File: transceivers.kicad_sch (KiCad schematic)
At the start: 18 parts, among them U401 TLE9351VSJ, U402 TLE7258SJ

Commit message: completed schematic
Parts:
- removed D33: BAT60A, Diode_SMD:D_SOD-323, symbol Diode:BAT60A
- added D513: PMEG4010CEH, Diode_SMD:D_SOD-123F, symbol Diode:PMEG4010CEH
- D401: value D_TVS_Dual_AAC -> PESD2CANFD24V-T
- FL401: value Filter_EMI_LL_1423 -> WE 744222
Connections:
- net Vdrive: now also D513.2 (A)
- net at R406.1: now also D513.1 (K)
- net +3V3 renamed +3.3V
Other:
- note removed: "ToDo: Drossel dimensionieren (Würth 744222?) TVS: PESD1CAN einfügen"
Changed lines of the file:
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@@
 (kicad_sch (version 20230121) (generator eeschema)
   (paper "A4")
+  (bus_alias "CAN" (members "CAN_TX" "CAN_RX" "CAN_STBY"))
   (bus_alias "Comm" (members "CAN_H" "CAN_L" "LIN"))
-  (bus_alias "CAN" (members "CAN_TX" "CAN_RX" "CAN_STBY"))
+  (bus_alias "Power_OUT" (members "Half0_OUT" "Half1_OUT" "1A_Out0" "1A_Out2" "1A_Out3" "1A_Out1" ""))
   (bus_alias "LIN" (members "LIN_TX" "LIN_RX" "LIN_EN"))
-  (bus_alias "Power_OUT" (members "Half0_OUT" "Half1_OUT" "1A_Out0" "1A_Out2" "1A_Out3" "1A_Out1" ""))
   (junction (at 166.37 99.06) (diameter 0) (color 0 0 0 0)
   )
@@
   (wire (pts (xy 58.42 58.42) (xy 71.12 58.42))
     (stroke (width 0) (type default))
-  )
-  (text "ToDo:\nDrossel dimensionieren (Würth 744222?)\nTVS: PESD1CAN einfügen"
-    (at 189.23 59.69 0)
-    (effects (font (size 1.27 1.27)) (justify left bottom))
   )
   (label "LIN_EN" (at 106.68 99.06 0) (fields_autoplaced)
@@
     )
   )
-  (symbol (lib_id "Device:R") (at 191.77 44.45 0) (unit 1)
-    (in_bom yes) (on_board yes) (dnp no) (fields_autoplaced)
-    (property "Reference" "R403" (at 194.31 43.1799 0)
-      (effects (font (size 1.27 1.27)) (justify left))
-    )
-    (property "Value" "60" (at 194.31 45.7199 0)
-      (effects (font (size 1.27 1.27)) (justify left))
-    )
-    (property "Footprint" "Resistor_SMD:R_0603_1608Metric" (at 189.992 44.45 90)
+  (symbol (lib_id "Device:R") (at 191.77 44.45 0) (mirror y) (unit 1)
+    (in_bom yes) (on_board yes) (dnp no)
+    (property "Reference" "R403" (at 189.23 43.1799 0)
+      (effects (font (size 1.27 1.27)) (justify left))
+    )
+    (property "Value" "60" (at 189.23 45.7199 0)
+      (effects (font (size 1.27 1.27)) (justify left))
+    )
+    (property "Footprint" "Resistor_SMD:R_0603_1608Metric" (at 193.548 44.45 90)
       (effects (font (size 1.27 1.27)) hide)
     )
@@
   )
   (symbol (lib_id "Device:Filter_EMI_LL_1423") (at 172.72 38.1 0) (unit 1)
-    (in_bom yes) (on_board yes) (dnp no) (fields_autoplaced)
-    (property "Reference" "FL401" (at 172.339 30.48 0)
-      (effects (font (size 1.27 1.27)))
-    )
-    (property "Value" "Filter_EMI_LL_1423" (at 172.339 33.02 0)
+    (in_bom yes) (on_board yes) (dnp no)
+    (property "Reference" "FL401" (at 172.72 43.18 0)
+      (effects (font (size 1.27 1.27)))
+    )
+    (property "Value" "WE 744222" (at 172.72 45.72 0)
       (effects (font (size 1.27 1.27)))
     )
@@
     )
   )
-  (symbol (lib_id "Device:R") (at 172.72 50.8 90) (unit 1)
-    (in_bom yes) (on_board yes) (dnp yes) (fields_autoplaced)
-    (property "Reference" "R404" (at 172.72 44.45 90)
-      (effects (font (size 1.27 1.27)))
-    )
-    (property "Value" "0" (at 172.72 46.99 90)
-      (effects (font (size 1.27 1.27)))
-    )
-    (property "Footprint" "Resistor_SMD:R_0603_1608Metric" (at 172.72 52.578 90)
+  (symbol (lib_id "Device:R") (at 172.72 50.8 90) (mirror x) (unit 1)
+    (in_bom yes) (on_board yes) (dnp yes)
+    (property "Reference" "R404" (at 172.72 57.15 90)
+      (effects (font (size 1.27 1.27)))
+    )
+    (property "Value" "0" (at 172.72 54.61 90)
+      (effects (font (size 1.27 1.27)))
+    )
+    (property "Footprint" "Resistor_SMD:R_0603_1608Metric" (at 172.72 49.022 90)
       (effects (font (size 1.27 1.27)) hide)
     )
@@
   )
   (symbol (lib_id "Device:D_TVS_Dual_AAC") (at 222.25 38.1 90) (unit 1)
-    (in_bom yes) (on_board yes) (dnp no) (fields_autoplaced)
-    (property "Reference" "D401" (at 219.71 36.8299 90)
-      (effects (font (size 1.27 1.27)) (justify left))
-    )
-    (property "Value" "D_TVS_Dual_AAC" (at 219.71 39.3699 90)
-      (effects (font (size 1.27 1.27)) (justify left))
+    (in_bom yes) (on_board yes) (dnp no)
+    (property "Reference" "D401" (at 226.06 41.91 90)
+      (effects (font (size 1.27 1.27)) (justify right))
+    )
+    (property "Value" "PESD2CANFD24V-T\n" (at 226.06 44.45 90)
+      (effects (font (size 1.27 1.27)) (justify right))
     )
     (property "Footprint" "Package_TO_SOT_SMD:SOT-23-3" (at 222.25 41.91 0)
@@
     )
   )
-  (symbol (lib_id "Device:R") (at 191.77 31.75 0) (unit 1)
-    (in_bom yes) (on_board yes) (dnp no) (fields_autoplaced)
-    (property "Reference" "R402" (at 194.31 30.4799 0)
-      (effects (font (size 1.27 1.27)) (justify left))
-    )
-    (property "Value" "60" (at 194.31 33.0199 0)
-      (effects (font (size 1.27 1.27)) (justify left))
-    )
-    (property "Footprint" "Resistor_SMD:R_0603_1608Metric" (at 189.992 31.75 90)
+  (symbol (lib_id "Device:R") (at 191.77 31.75 0) (mirror y) (unit 1)
+    (in_bom yes) (on_board yes) (dnp no)
+    (property "Reference" "R402" (at 189.23 30.4799 0)
+      (effects (font (size 1.27 1.27)) (justify left))
+    )
+    (property "Value" "60" (at 189.23 33.0199 0)
+      (effects (font (size 1.27 1.27)) (justify left))
+    )
+    (property "Footprint" "Resistor_SMD:R_0603_1608Metric" (at 193.548 31.75 90)
       (effects (font (size 1.27 1.27)) hide)
     )
@@
         (path "/e63e39d7-6ac0-4ffd-8aa3-1841a4541b55/9985b1d8-396b-4387-8a13-f50cc48ebb06"
           (reference "R25") (unit 1)
-        )
-      )
-    )
-  )
-  (symbol (lib_id "Diode:BAT60A") (at 166.37 82.55 90) (unit 1)
-    (in_bom yes) (on_board yes) (dnp no) (fields_autoplaced)
-    (property "Reference" "D33" (at 168.91 82.2325 90)
-      (effects (font (size 1.27 1.27)) (justify right))
-    )
-    (property "Value" "BAT60A" (at 168.91 84.7725 90)
-      (effects (font (size 1.27 1.27)) (justify right))
-    )
-    (property "Footprint" "Diode_SMD:D_SOD-323" (at 170.815 82.55 0)
-      (effects (font (size 1.27 1.27)) hide)
-    )
-    (property "Datasheet" "https://www.infineon.com/dgdl/Infineon-BAT60ASERIES-DS-v01_01-en.pdf?fileId=db3a304313d846880113def70c9304a9" (at 166.37 82.55 0)
-      (effects (font (size 1.27 1.27)) hide)
-    )
-    (pin "1")
-    (pin "2")
-    (instances
-      (project "Sensor_Board"
-        (path "/e2a0eb17-0eae-4cdd-befd-118f8728b921/8460c5f0-f567-411d-b3a7-76d8207879f4"
-          (reference "D33") (unit 1)
-        )
-        (path "/e2a0eb17-0eae-4cdd-befd-118f8728b921"
-          (reference "D21") (unit 1)
-        )
-        (path "/e2a0eb17-0eae-4cdd-befd-118f8728b921/76b65cb7-064b-4e1a-ab08-2030a37ece9c"
-          (reference "D1205") (unit 1)
-        )
-        (path "/e2a0eb17-0eae-4cdd-befd-118f8728b921/c1280e85-b203-4b6b-82d8-dbf0409d7c4d"
-          (reference "D501") (unit 1)
-        )
-        (path "/e2a0eb17-0eae-4cdd-befd-118f8728b921/3da51442-cf5a-4c82-94bf-5b28220d11d0"
-          (reference "D402") (unit 1)
-        )
-      )
-      (project "FT22_VCU_Konzept"
-        (path "/e63e39d7-6ac0-4ffd-8aa3-1841a4541b55/3c48a9d0-891a-4016-826f-62373ede344c"
-          (reference "D33") (unit 1)
         )
       )
@@
         )
       )
+    )
+  )
+  (symbol (lib_id "Diode:PMEG4010CEH") (at 166.37 82.55 90) (unit 1)
+    (in_bom yes) (on_board yes) (dnp no) (fields_autoplaced)
+    (property "Reference" "D513" (at 168.91 82.2325 90)
+      (effects (font (size 1.27 1.27)) (justify right))
+    )
+    (property "Value" "PMEG4010CEH" (at 168.91 84.7725 90)
+      (effects (font (size 1.27 1.27)) (justify right))
+    )
+    (property "Footprint" "Diode_SMD:D_SOD-123F" (at 170.815 82.55 0)
+      (effects (font (size 1.27 1.27)) hide)
+    )
+    (property "Datasheet" "https://assets.nexperia.com/documents/data-sheet/PMEG4010CEH_PMEG4010CEJ.pdf" (at 166.37 82.55 0)
+      (effects (font (size 1.27 1.27)) hide)
+    )
+    (pin "1")
+    (pin "2")
+    (instances
+      (project "Sensor_Board"
+        (path "/e2a0eb17-0eae-4cdd-befd-118f8728b921/c1280e85-b203-4b6b-82d8-dbf0409d7c4d"
+          (reference "D513") (unit 1)
+        )
+        (path "/e2a0eb17-0eae-4cdd-befd-118f8728b921/3da51442-cf5a-4c82-94bf-5b28220d11d0"
+          (reference "D402") (unit 1)
+        )
+      )

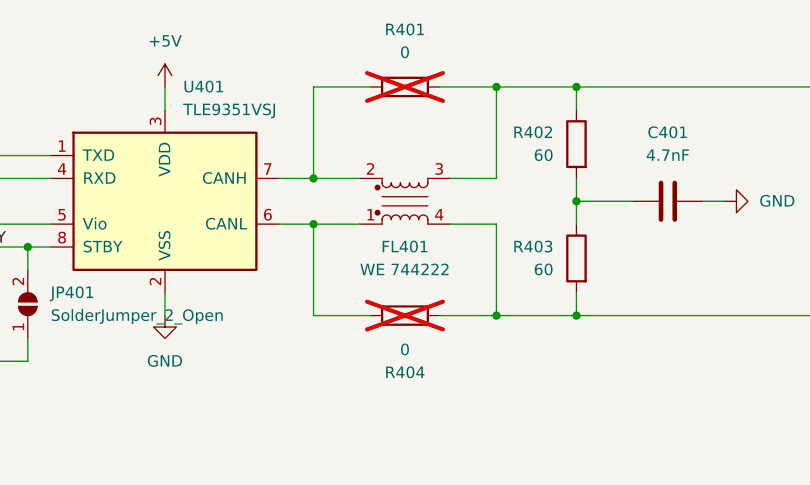
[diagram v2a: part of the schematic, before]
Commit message: placed components and began routing
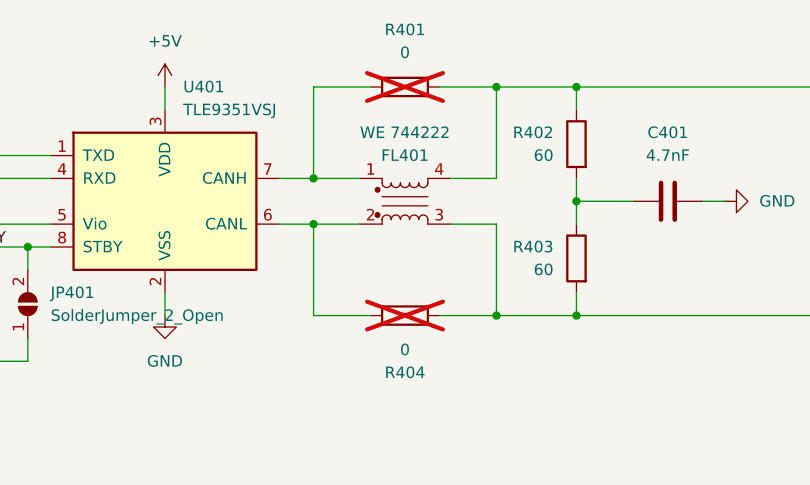
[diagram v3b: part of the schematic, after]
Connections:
- net CAN_H: now also FL401.4; no longer FL401.3
- net CAN_L: now also FL401.3; no longer FL401.4
- net at R404.1, U401.6 (CANL): now also FL401.2; no longer FL401.1
- net at R401.1, U401.7 (CANH): now also FL401.1; no longer FL401.2
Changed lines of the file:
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@@
 (kicad_sch (version 20230121) (generator eeschema)
   (paper "A4")
+  (bus_alias "Power_OUT" (members "Half0_OUT" "Half1_OUT" "1A_Out0" "1A_Out2" "1A_Out3" "1A_Out1" ""))
+  (bus_alias "LIN" (members "LIN_TX" "LIN_RX" "LIN_EN"))
   (bus_alias "CAN" (members "CAN_TX" "CAN_RX" "CAN_STBY"))
   (bus_alias "Comm" (members "CAN_H" "CAN_L" "LIN"))
-  (bus_alias "Power_OUT" (members "Half0_OUT" "Half1_OUT" "1A_Out0" "1A_Out2" "1A_Out3" "1A_Out1" ""))
-  (bus_alias "LIN" (members "LIN_TX" "LIN_RX" "LIN_EN"))
   (junction (at 166.37 99.06) (diameter 0) (color 0 0 0 0)
   )
@@
     )
   )
-  (symbol (lib_id "Device:Filter_EMI_LL_1423") (at 172.72 38.1 0) (unit 1)
+  (symbol (lib_id "Device:Filter_EMI_LL_1423") (at 172.72 38.1 0) (mirror x) (unit 1)
     (in_bom yes) (on_board yes) (dnp no)
-    (property "Reference" "FL401" (at 172.72 43.18 0)
-      (effects (font (size 1.27 1.27)))
-    )
-    (property "Value" "WE 744222" (at 172.72 45.72 0)
-      (effects (font (size 1.27 1.27)))
-    )
-    (property "Footprint" "Inductor_SMD:L_CommonMode_Wuerth_WE-SL2" (at 172.72 44.45 0)
-      (effects (font (size 1.27 1.27)) hide)
-    )
-    (property "Datasheet" "~" (at 172.72 37.084 90)
-      (effects (font (size 1.27 1.27)) hide)
-    )
+    (property "Reference" "FL401" (at 172.72 33.02 0)
+      (effects (font (size 1.27 1.27)))
+    )
+    (property "Value" "WE 744222" (at 172.72 30.48 0)
+      (effects (font (size 1.27 1.27)))
+    )
+    (property "Footprint" "Inductor_SMD:L_CommonMode_Wuerth_WE-SL2" (at 172.72 31.75 0)
+      (effects (font (size 1.27 1.27)) hide)
+    )
+    (property "Datasheet" "~" (at 172.72 39.116 90)
+      (effects (font (size 1.27 1.27)) hide)
+    )

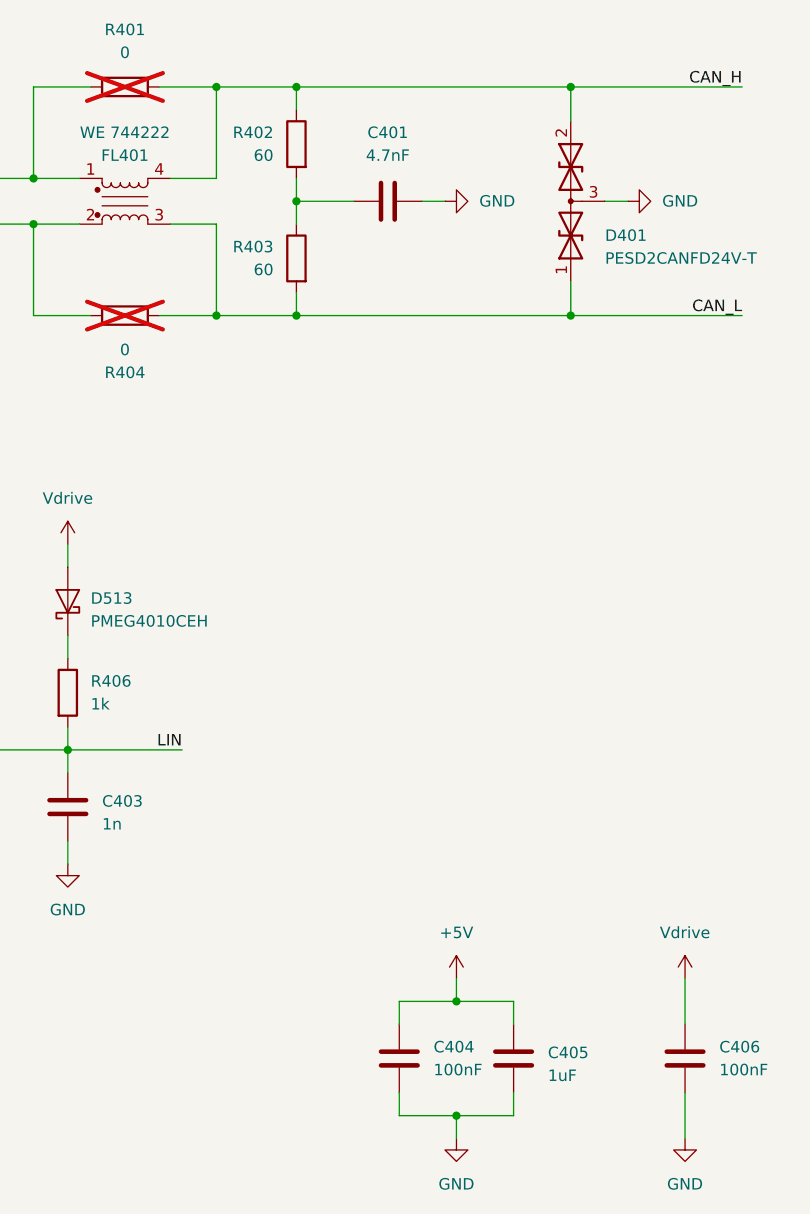
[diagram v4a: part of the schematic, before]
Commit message: fixed oscillator and component values
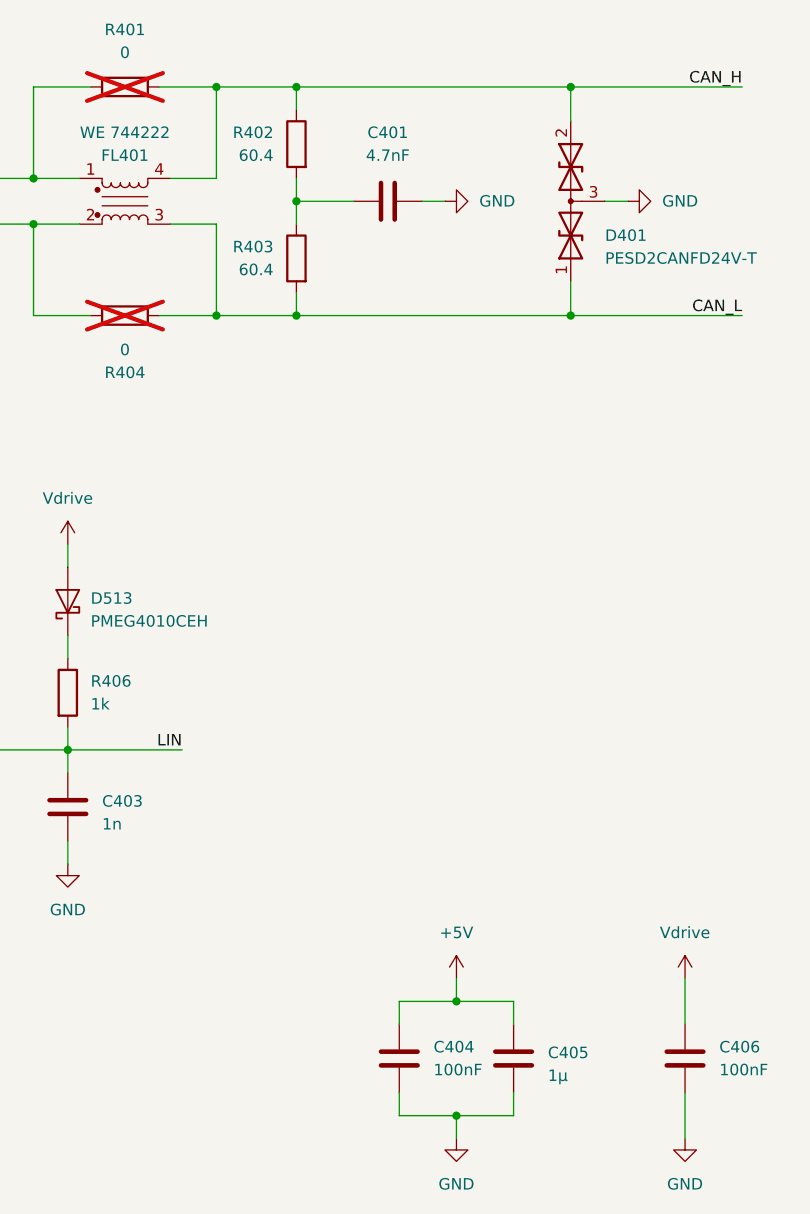
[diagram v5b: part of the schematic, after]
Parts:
- C405: value 1uF -> 1µ
- R402, R403: value 60 -> 60.4
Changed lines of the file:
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@@
   (bus_alias "LIN" (members "LIN_TX" "LIN_RX" "LIN_EN"))
   (bus_alias "Power_OUT" (members "Half0_OUT" "Half1_OUT" "1A_Out0" "1A_Out2" "1A_Out3" "1A_Out1" ""))
+  (bus_alias "Comm" (members "CAN_H" "CAN_L" "LIN"))
   (bus_alias "CAN" (members "CAN_TX" "CAN_RX" "CAN_STBY"))
-  (bus_alias "Comm" (members "CAN_H" "CAN_L" "LIN"))
   (junction (at 166.37 99.06) (diameter 0) (color 0 0 0 0)
   )
@@
       (effects (font (size 1.27 1.27)) (justify left))
     )
-    (property "Value" "1uF" (at 219.71 135.255 0)
+    (property "Value" "1µ" (at 219.71 135.255 0)
       (effects (font (size 1.27 1.27)) (justify left))
     )
@@
       (effects (font (size 1.27 1.27)) (justify left))
     )
-    (property "Value" "60" (at 189.23 45.7199 0)
+    (property "Value" "60.4" (at 189.23 45.7199 0)
       (effects (font (size 1.27 1.27)) (justify left))
     )
@@
       (effects (font (size 1.27 1.27)) (justify left))
     )
-    (property "Value" "60" (at 189.23 33.0199 0)
-      (effects (font (size 1.27 1.27)) (justify left))
-    )
+    (property "Value" "60.4" (at 189.23 33.0199 0)
+      (effects (font (size 1.27 1.27)) (justify left))
+    )
